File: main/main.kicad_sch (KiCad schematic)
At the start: 25 parts, among them J1 USB_C_Receptacle_USB2.0, J2 TC2030_SWD, U1 STM32L063C8Tx, U2 SN74LV1T34DBV, U3 WE-TVS-82400102, U4 MIC5504-3.3YMT

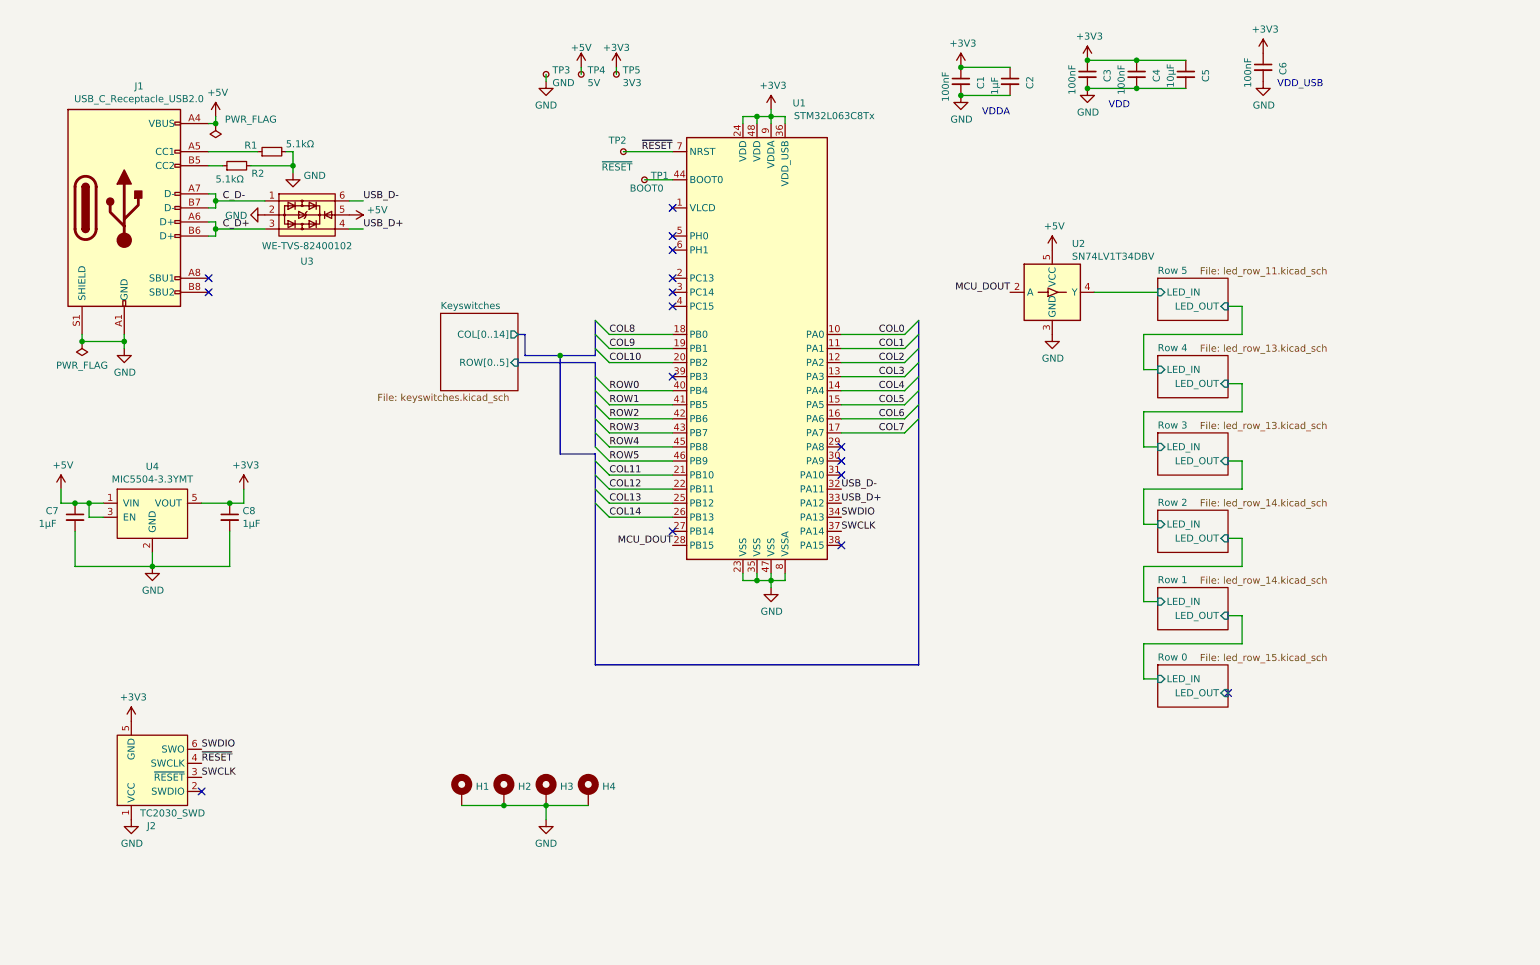
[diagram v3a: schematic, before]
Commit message: Convert to kicad 6.0
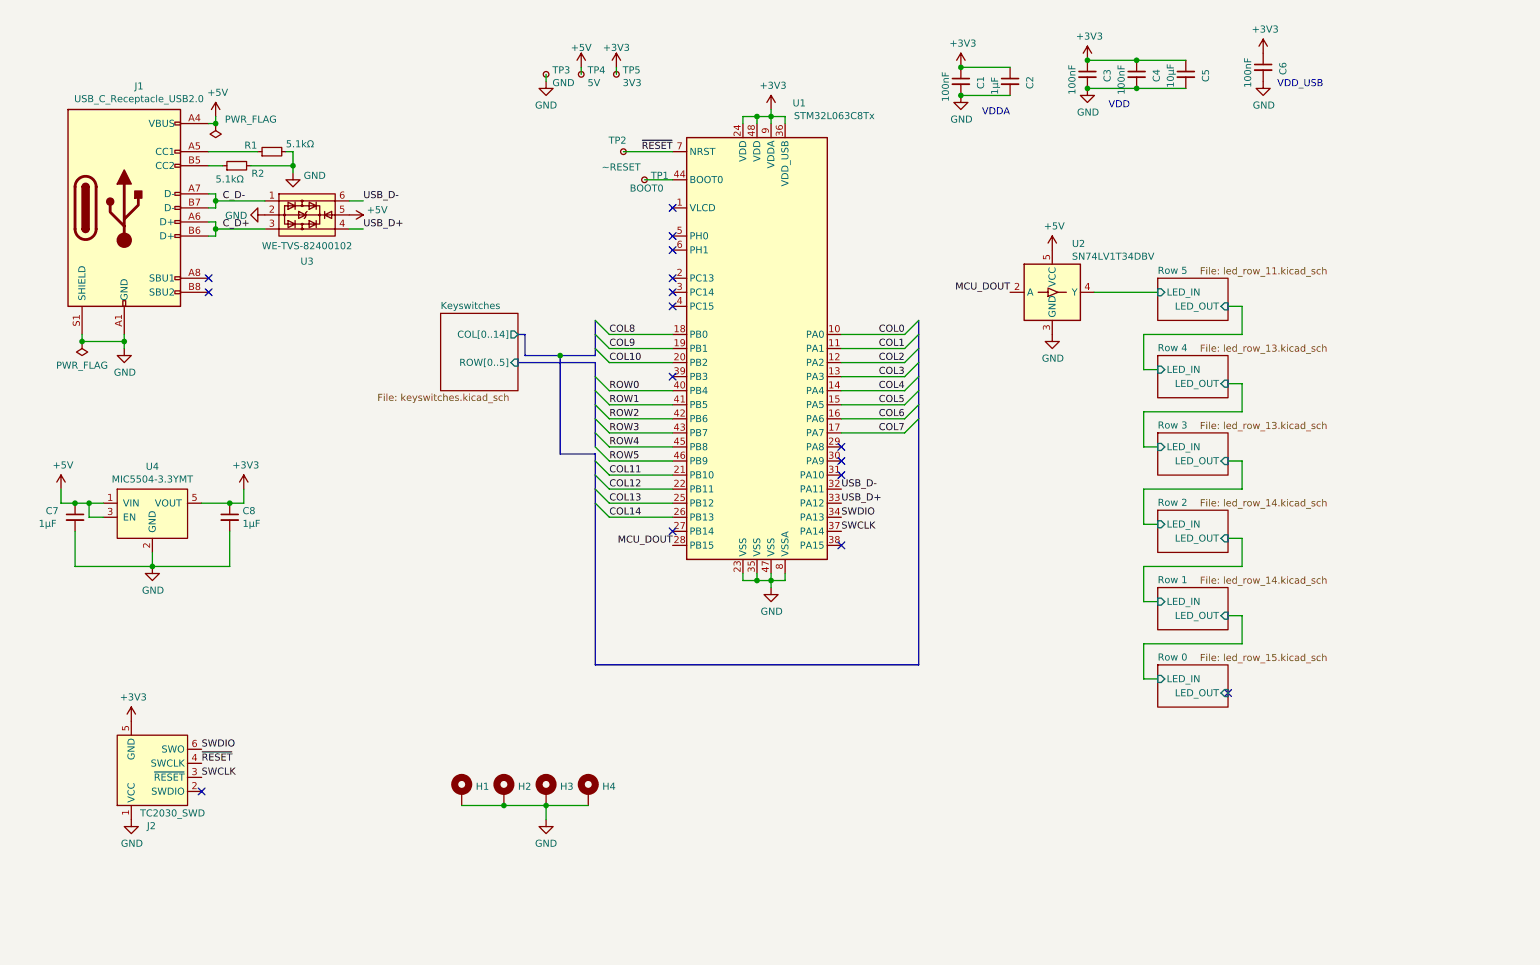
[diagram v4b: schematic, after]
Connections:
- net ~RESET renamed ~{RESET}

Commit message: Switch to nRF58420 module and battery power
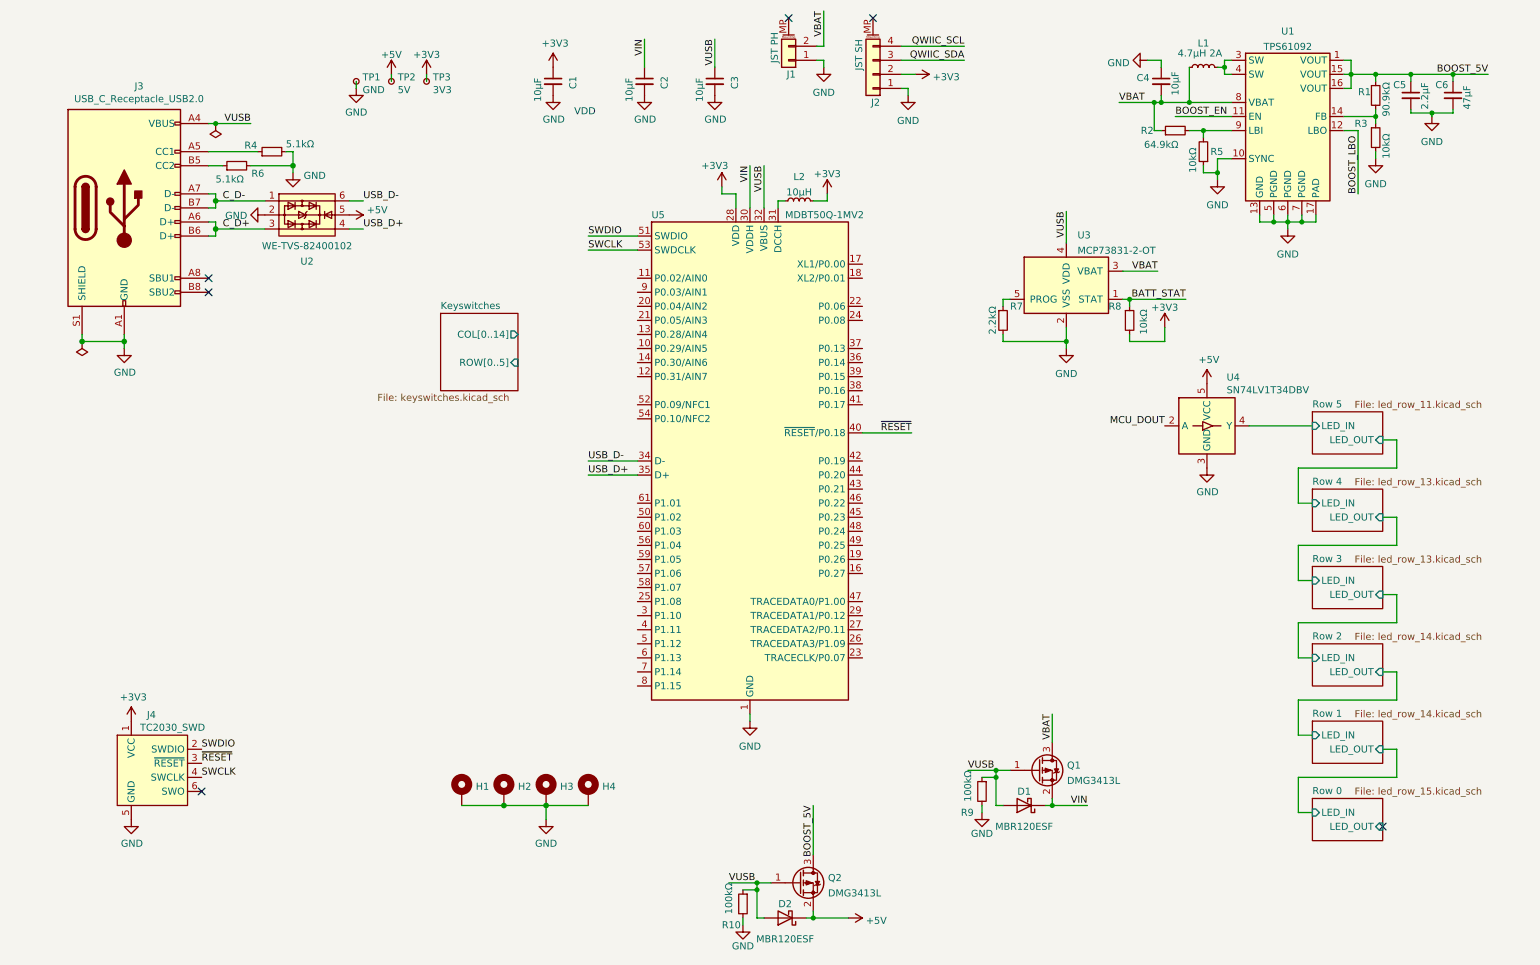
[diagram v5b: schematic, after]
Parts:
- removed C7, C8: 1µF, Capacitor_SMD:C_0603_1608Metric, symbol Device:C_Small
- removed TP1: BOOT0, TestPoint:TestPoint_Pad_D1.0mm, symbol Connector:TestPoint_Small
- removed TP2: ~RESET, TestPoint:TestPoint_Pad_D1.0mm, symbol Connector:TestPoint_Small
- removed U1: STM32L063C8Tx, Package_QFP:LQFP-48_7x7mm_P0.5mm, symbol MCU_ST_STM32L0:STM32L063C8Tx
- removed U4: MIC5504-3.3YMT, Package_TO_SOT_SMD:SOT-23-5, symbol chonc60:MIC550x
- added D1, D2: MBR120ESF, Diode_SMD:D_SOD-123F, symbol Device:D_Schottky
- added J1: JST PH, Connector_JST:JST_PH_S2B-PH-SM4-TB_1x02-1MP_P2.00mm_Horizontal, symbol Connector_Generic_MountingPin:Conn_01x02_MountingPin
- added J2: JST SH, Connector_JST:JST_SH_SM04B-SRSS-TB_1x04-1MP_P1.00mm_Horizontal, symbol Connector_Generic_MountingPin:Conn_01x04_MountingPin
- added L1: 4.7µH 2A, Inductor_SMD:L_Taiyo-Yuden_NR-50xx, symbol Device:L_Small
- added L2: 10µH, Inductor_SMD:L_0603_1608Metric, symbol Device:L_Small
- added Q1, Q2: DMG3413L, Package_TO_SOT_SMD:SOT-23, symbol Device:Q_PMOS_GSD
- added R1: 90.9kΩ, Resistor_SMD:R_0603_1608Metric, symbol Device:R_Small
- added R10, R9: 100kΩ, Resistor_SMD:R_0603_1608Metric, symbol Device:R_Small
- added R2: 64.9kΩ, Resistor_SMD:R_0603_1608Metric, symbol Device:R_Small
- added R3, R5, R8: 10kΩ, Resistor_SMD:R_0603_1608Metric, symbol Device:R_Small
- added R7: 2.2kΩ, Resistor_SMD:R_0603_1608Metric, symbol Device:R_Small
- added U1: TPS61092, Package_DFN_QFN:Texas_S-PVQFN-N16_EP2.7x2.7mm_ThermalVias, symbol Regulator_Switching:TPS61092
- added U3: MCP73831-2-OT, Package_TO_SOT_SMD:SOT-23-5, symbol Battery_Management:MCP73831-2-OT
- added U5: MDBT50Q-1MV2, RF_Module:Raytac_MDBT50Q, symbol RF_Module:MDBT50Q-1MV2
- C1, C3, C4: value 100nF -> 10µF
- C2: value 1µF -> 10µF
- C5: value 10µF -> 2.2µF
- C6: value 100nF -> 47µF
- renumbered J1 to J3, J2 to J4, R1 to R4, R2 to R6, TP3 to TP1, TP4 to TP2, TP5 to TP3, U3 to U2, U2 to U4
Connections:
- net +3V3: now also J4.1 (VCC), J2.2 (Pin_2), L2.2, R8.2, U5.28 (VDD); no longer C2.1, C3.1, C4.1, C5.1, C6.1, J4.5 (GND)
- net +5V: now also D2.1 (K), Q2.2 (S); no longer J3.A4 (VBUS), J3.A9 (VBUS), J3.B4 (VBUS), J3.B9 (VBUS)
- net GND: now also C4.1, J4.5 (GND), J1.1 (Pin_1), J2.1 (Pin_1), R10.2, R3.2, R5.1, R7.2, R9.2, U1.10 (SYNC), U1.13 (GND), U1.17 (PAD), U1.5 (PGND), U1.6 (PGND), U1.7 (PGND), U3.2 (VSS), U5.1 (GND), U5.15 (GND), U5.2 (GND), U5.33 (GND), U5.55 (GND); no longer C4.2, J4.1 (VCC)
- net SWCLK: now also J4.4 (SWCLK), U5.53 (SWDCLK); no longer J4.3 (~{RESET})
- net SWDIO: now also J4.2 (SWDIO), U5.51 (SWDIO); no longer J4.6 (SWO)
- net USB_D+: now also U5.35 (D+)
- net USB_D-: now also U5.34 (D-)
- net ~{RESET}: now also J4.3 (~{RESET}), U5.40 (~{RESET}/P0.18); no longer J4.4 (SWCLK)
- new net: L1.2, U1.3 (SW), U1.4 (SW)
- new net: R1.2, R3.1, U1.14 (FB)
- new net: L2.1, U5.31 (DCCH)
- new net: R2.2, R5.2, U1.9 (LBI)
- new net: R7.1, U3.5 (PROG)
- new net BATT_STAT: R8.1, U3.1 (STAT)
- new net BOOST_5V: C5.1, C6.1, Q2.3 (D), R1.1, U1.1 (VOUT), U1.15 (VOUT), U1.16 (VOUT)
- new net BOOST_EN: U1.11 (EN)
- new net BOOST_LBO: U1.12 (LBO)
- new net QWIIC_SCL: J2.4 (Pin_4)
- new net QWIIC_SDA: J2.3 (Pin_3)
- new net VBAT: C4.2, J1.2 (Pin_2), L1.1, Q1.3 (D), R2.1, U1.8 (VBAT), U3.3 (VBAT)
- new net VIN: C2.1, D1.1 (K), Q1.2 (S), U5.30 (VDDH)
- new net VUSB: C3.1, D1.2 (A), D2.2 (A), J3.A4 (VBUS), J3.A9 (VBUS), J3.B4 (VBUS), J3.B9 (VBUS), Q1.1 (G), Q2.1 (G), R10.1, R9.1, U3.4 (VDD), U5.32 (VBUS)
- no-connect marks 16 -> 6
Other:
- note removed: "VDDA"
- note removed: "VDD_USB"
- moved on the sheet: C1, TP1, TP2, TP3, U4

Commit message: routing work
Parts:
- added C87, C88: 22pF, Capacitor_SMD:C_0603_1608Metric, symbol Device:C_Small
- added Y1: 32.768kHz, Crystal:Crystal_SMD_3215-2Pin_3.2x1.5mm, symbol Device:Crystal_Small
- C6: footprint Capacitor_SMD:C_0603_1608Metric -> Capacitor_SMD:C_0805_2012Metric
- J4: footprint Connector:Tag-Connect_TC2030-IDC-NL_2x03_P1.27mm_Vertical -> Connector:Tag-Connect_TC2030-IDC-FP_2x03_P1.27mm_Vertical
- R1, R2, R3, R5: footprint Resistor_SMD:R_0603_1608Metric -> Resistor_SMD:R_0402_1005Metric
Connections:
- net Row 5/LED_IN is gone; now on net Row 0/LED_IN: U4.4 (Y)
- net +5V: no longer U2.5
- net GND: now also C87.2, C88.2
- net VUSB: now also U2.5
- net at U5.17 (XL1/P0.00): now also C87.1, Y1.2
- net at U5.18 (XL2/P0.01): now also C88.1, Y1.1
- net COL1: now reaches U5.26 (TRACEDATA3/P1.09)
- net COL0: now reaches U5.27 (TRACEDATA2/P0.11)

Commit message: Connect up MCU
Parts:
- added R11, R12: 5.1kΩ, Resistor_SMD:R_0603_1608Metric, symbol Device:R_Small
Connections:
- net +3V3: now also R11.1, R12.1
- net COL0: now also U5.49 (P0.25); no longer U5.27 (TRACEDATA2/P0.11)
- net COL1: now also U5.48 (P0.24); no longer U5.26 (TRACEDATA3/P1.09)
- net MCU_DOUT: now also U5.19 (P0.26)
- net QWIIC_SCL: now also U5.36 (P0.14), R11.2
- net QWIIC_SDA: now also U5.38 (P0.16), R12.2
- net ROW5: now reaches U5.22 (P0.06)
- net ROW4: now reaches U5.23 (TRACECLK/P0.07)
- net ROW3: now reaches U5.24 (P0.08)
- net ROW2: now reaches U5.25 (P1.08)
- net COL14: now reaches U5.3 (P1.10)
- net COL13: now reaches U5.4 (P1.11)
- net COL7: now reaches U5.42 (P0.19)
- net COL6: now reaches U5.43 (P0.21)
- net COL5: now reaches U5.44 (P0.20)
- net COL4: now reaches U5.45 (P0.23)
- net COL3: now reaches U5.46 (P0.22)
- net COL2: now reaches U5.47 (TRACEDATA0/P1.00)
- net COL12: now reaches U5.5 (P1.12)
- net COL11: now reaches U5.6 (P1.13)
- net COL10: now reaches U5.7 (P1.14)
- net COL9: now reaches U5.8 (P1.15)
- net COL8: now reaches U5.9 (P0.03/AIN1)
- new net ROW0: U5.27 (TRACEDATA2/P0.11)
- new net ROW1: U5.26 (TRACEDATA3/P1.09)
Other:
- moved on the sheet: C87, C88, J4, R7, R8, U3, U4, Y1
